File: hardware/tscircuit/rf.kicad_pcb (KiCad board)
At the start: 2 copper layers, 120 x 90 mm, 28 parts, among them Y1 Y1

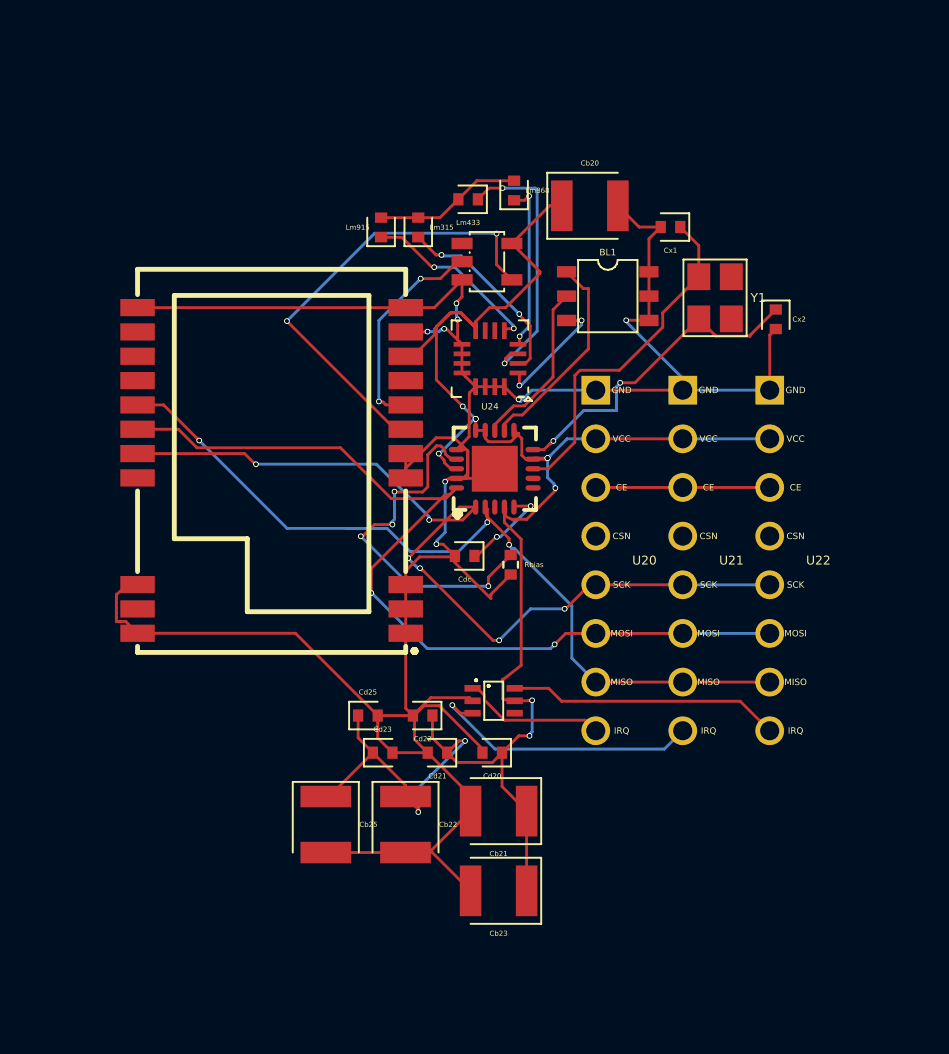
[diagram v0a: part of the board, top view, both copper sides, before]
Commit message: hw(rf,c5-buses): resolve SP4T sourcing — SKY13414 (in stock) + RFSW_C
PE42440 isn't stocked at JLCPCB; swapped to the in-stock SKY13414-485LF (C255353),
engine-pulled footprint. It uses 3-line control (V1/V2/V3 = RFSW_A/RFSW_B/RFSW_C);
added RFSW_C on PCA9555 #2 P07 (c5-buses). Switch common -> CC1101 radio, RF1..RF4 ->
per-band matches -> shared antenna; EP + unused pads grounded. Both sheets KiCad DRC
0 unconnected / 0 shorts / 0 parity. Docs (rf EN+RU) updated.

Co-Authored-By: Claude Opus 4.8 <noreply@anthropic.com>
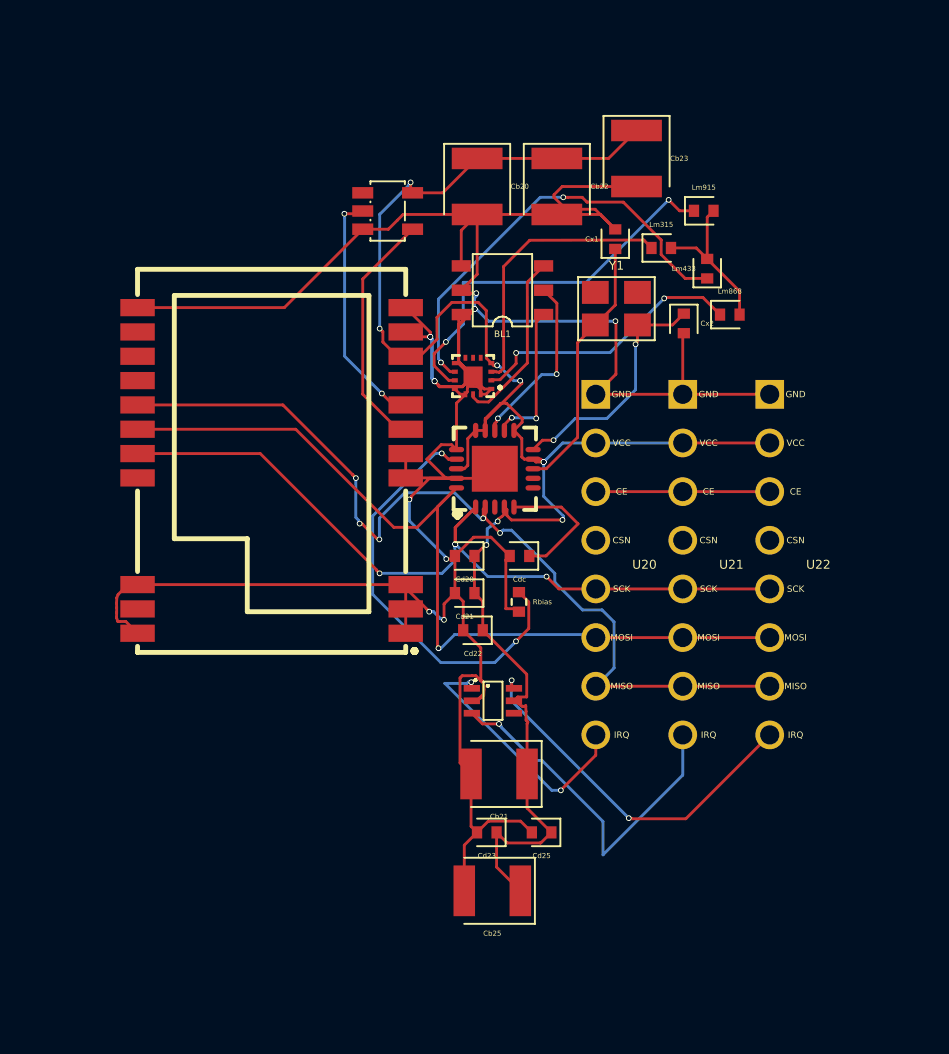
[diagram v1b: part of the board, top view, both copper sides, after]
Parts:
- U24: footprint tscircuit:chip_qfn16 -> tscircuit:chip
- moved Cb23 38.9 mm to (119.0, 83.7), turned to -90 degrees
- moved Cb22 34.2 mm to (114.9, 85.2)
- moved Lm915 16.9 mm to (122.6, 86.4), turned to 0 degrees
- moved Lm433 13.0 mm to (122.7, 89.5), turned to 90 degrees
- moved Lm868 13.0 mm to (123.9, 91.9), turned to 0 degrees
- moved Lm315 12.7 mm to (120.3, 88.4), turned to 0 degrees
- moved Cd25 10.9 mm to (114.1, 118.9), turned to 180 degrees
- moved Cd20 10.4 mm to (110.1, 104.5)
- moved Cb25 9.35 mm to (111.5, 121.9), turned to 180 degrees
- moved Cd21 8.45 mm to (110.1, 106.4)
- moved Cd23 6.85 mm to (111.2, 118.9), turned to 180 degrees
- moved Cb20 5.97 mm to (110.7, 85.2), turned to -90 degrees
- moved U27 5.82 mm to (106.1, 86.5)
- moved BL1 5.51 mm to (112.0, 90.6), turned to 180 degrees
- moved Y1 5.18 mm to (118.0, 91.6), turned to 0 degrees
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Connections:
- U24 pad 1: CC1101_RF -> GND
- U24 pad 10: GND -> .U24 > .RF4 to .Lm915 > .pin1
- U24 pad 13: GND -> CC1101_RF
- U24 pad 2: .U24 > .RF1 to .Lm315 > .pin1 -> .U24 > .RF3 to .Lm868 > .pin1
- U24 pad 3: .U24 > .RF2 to .Lm433 > .pin1 -> .U24 > .RF1 to .Lm315 > .pin1
- U24 pad 4: .U24 > .RF3 to .Lm868 > .pin1 -> V3V3
- U24 pad 5: .U24 > .RF4 to .Lm915 > .pin1 -> RFSW_C
- U24 pad 6: RFSW_A -> RFSW_B
- U24 pad 7: RFSW_B -> RFSW_A
- U24 pad 8: V3V3 -> GND
- U24 pad 9: GND -> .U24 > .RF2 to .Lm433 > .pin1
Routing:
- net GND: track 148.8 -> 179.6 mm, vias 8 -> 12
- net LoRa_RXEN: track 24.1 -> 12.7 mm, vias 2 -> 0
- net .U24 > .RF4 to .Lm915 > .pin1: track 9.50 -> 20.4 mm
- net .U24 > .RF2 to .Lm433 > .pin1: track 14.2 -> 22.7 mm
- net nRF24_1_IRQ: track 7.49 -> 13.8 mm, vias 0 -> 2
- net .U24 > .RF3 to .Lm868 > .pin1: track 8.85 -> 14.4 mm
- net nRF24_3_IRQ: track 14.2 -> 19.4 mm, vias 0 -> 2
- net .U23 > .XOSC_Q1 to .Y1 > .pin1: track 18.3 -> 13.7 mm
- net .U23 > .XOSC_Q2 to .Y1 > .pin2: track 17.2 -> 12.7 mm
- net SPI_MISO: track 43.6 -> 47.9 mm, vias 3 -> 5
- net nRF24_2_IRQ: track 14.6 -> 19.0 mm
- net .U24 > .RF1 to .Lm315 > .pin1: track 10.2 -> 14.5 mm, vias 2 -> 0
- net V3V3: track 99.3 -> 95.7 mm, vias 11 -> 9
- net SPI_SCK: track 45.9 -> 42.5 mm, vias 6 -> 4
- net .U23 > .RF_P to .BL1 > .RFP: track 11.0 -> 7.73 mm, vias 0 -> 2
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
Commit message: hw: fix 6 issues from realized-board self-review (2 blockers)
Adversarial multi-agent review of the real-parts board caught 6 real defects the
per-sheet DRC couldn't see; all datasheet-verified, fixed, sheets re-verified
(DRC parity=0 each):

- BLOCKER (power): BQ25887 SNS was tied to BAT externally -> shorts the internal
  charge-current shunt, defeating ICHG regulation on the 2S pack. SNS is now its own
  net (44uF to GND only); the SNS<->BAT shunt is internal.
- BLOCKER (expansion): PESD5V0S2UAT ESD arrays (common-cathode) had the common cathode
  on GND -> every I2C logic-high forward-biases the diode and clamps SDA/SCL to ~0.6V
  (whole bus dead). Cathode moved to +3V3 (clamps overshoot above the rail).
- MAJOR (audio): PAM8302 inputs were DC-coupled (IN- hard to GND) -> breaks the
  internal VDD/2 bias and rails the output. Added series 0.1uF caps on both inputs.
- MINOR (power): BQ25887 TS divider was missing RT2 (30.1k || NTC) -> shifted temp
  window; added.
- MINOR (power): MP2315 bootstraps were missing the datasheet-required 20R series
  resistor; added Rbst4/Rbst5.
- MINOR (rf): SP4T pins 1/8/11/12/14 are N/C per the SKY13414 datasheet -> untied from
  GND (only the EP paddle is ground).

GPIO45 (VDD_SPI strap on CC1101 GDO2) is handled by the set_flash_voltage eFuse (a
verifier false-positive) -> documented inline. Docs (power EN+RU) corrected.

Co-Authored-By: Claude Opus 4.8 <noreply@anthropic.com>
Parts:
- moved Lm868 24.7 mm to (99.6, 87.3), turned to 90 degrees
- moved Lm433 21.0 mm to (102.0, 85.8), turned to 180 degrees
- moved Lm315 18.3 mm to (102.0, 87.8), turned to 180 degrees
- moved Lm915 15.7 mm to (107.2, 83.2), turned to 180 degrees
- moved Cb23 0.13 mm to (119.0, 83.9)
- moved Cx1 0.13 mm to (117.9, 88.1)
- moved Cx2 0.13 mm to (121.5, 92.5)
- moved U20 0.13 mm to (116.9, 105.1)
- moved U21 0.13 mm to (121.5, 105.1)
- moved U22 0.13 mm to (126.0, 105.1)
- moved Y1 0.13 mm to (118.0, 91.7)
- moved BL1 0.05 mm to (112.0, 90.5)
- moved Cb20 0.05 mm to (110.7, 85.1)
- moved Cb22 0.05 mm to (114.9, 85.1)
- turned U24 to 0 degrees
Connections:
- U24 pad 1: GND -> (no net)
- U24 pad 11: GND -> (no net)
- U24 pad 12: GND -> (no net)
- U24 pad 14: GND -> (no net)
- U24 pad 8: GND -> (no net)
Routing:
- net V3V3: track 95.7 -> 125.0 mm, vias 9 -> 13
- net .U24 > .RF3 to .Lm868 > .pin1: track 14.4 -> 28.2 mm, vias 2 -> 4
- net GND: track 179.6 -> 171.3 mm, vias 12 -> 15
- net CC1101_RF: track 9.35 -> 17.6 mm, vias 0 -> 2
- net nRF24_1_IRQ: track 13.8 -> 7.83 mm, vias 2 -> 0
- net .U23 > .RBIAS to .Rbias > .pin1: track 22.4 -> 16.7 mm
- net ANT_CC1101: track 8.38 -> 12.7 mm
- net .U24 > .RF2 to .Lm433 > .pin1: track 22.7 -> 18.4 mm, vias 2 -> 4
- net LoRa_TR: track 12.7 -> 16.8 mm, vias 2 -> 0
- net nRF24_2_IRQ: track 19.0 -> 15.0 mm
- net nRF24_3_IRQ: track 19.4 -> 15.5 mm, vias 2 -> 0
- net SPI_SCK: track 42.5 -> 38.9 mm, vias 4 -> 3
- net SPI_MOSI: track 46.1 -> 43.1 mm, vias 1 -> 3
- net .U24 > .RF1 to .Lm315 > .pin1: track 14.5 -> 17.4 mm, vias 0 -> 6
- net .U24 > .RF4 to .Lm915 > .pin1: track 20.4 -> 18.3 mm
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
